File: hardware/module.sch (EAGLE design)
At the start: 118 parts, among them IC1 IC_USBLC6-2, IC2 LM1117IMPX-3.3, IC3 PIC32MX795F512, IC4 DP83848, IC5 LM1117MPX-2.5, U1 USD-SOCKETUSD, U2 VS1003, X2 CRYSTALS-NOGND-CFPX-217, X3 KUSBVX, Y3 CRYSTAL-GROUNDEDSMD-5X3.2

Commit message: Backlight fixed
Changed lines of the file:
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@@
 <pinref part="SV1" gate="G$1" pin="1"/>
 <wire x1="340.36" y1="243.84" x2="345.44" y2="243.84" width="0.1524" layer="91"/>
+<label x="345.44" y="243.84" size="1.4224" layer="95" xref="yes"/>
 </segment>
 </net>
@@
 <pinref part="SV1" gate="G$1" pin="2"/>
 <wire x1="325.12" y1="243.84" x2="320.04" y2="243.84" width="0.1524" layer="91"/>
+<label x="320.04" y="243.84" size="1.4224" layer="95" rot="R180" xref="yes"/>
 </segment>
 </net>

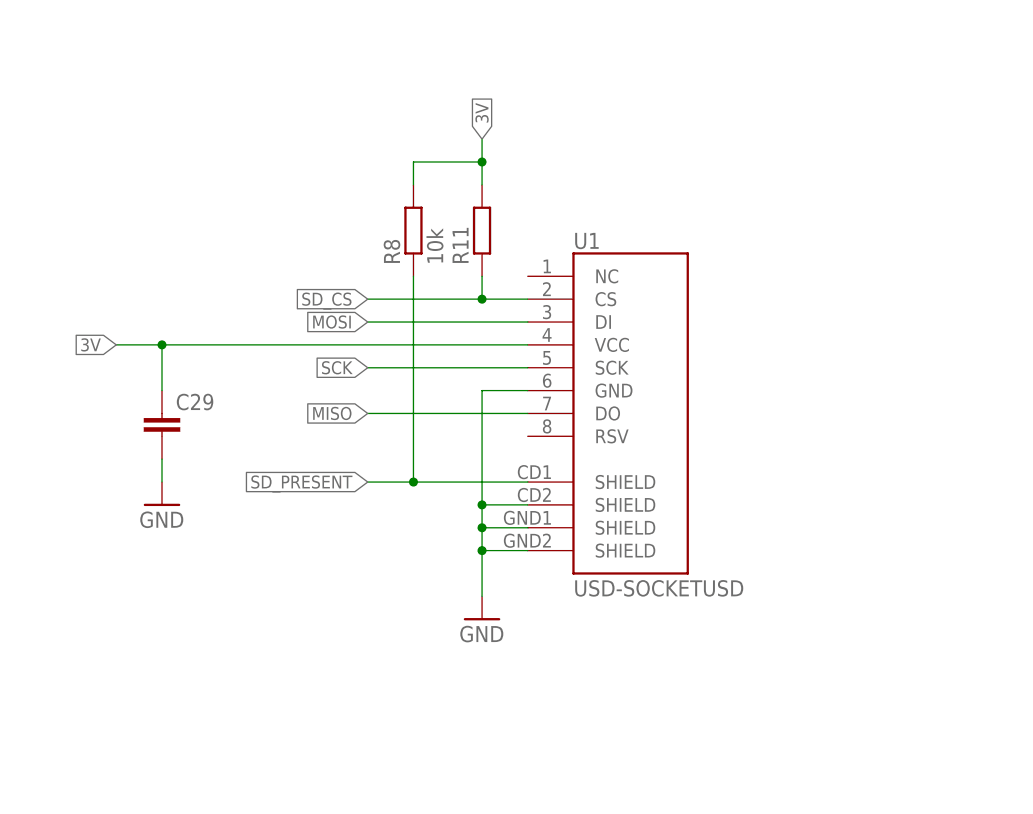
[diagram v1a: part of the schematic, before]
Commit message: MISO pull-up added
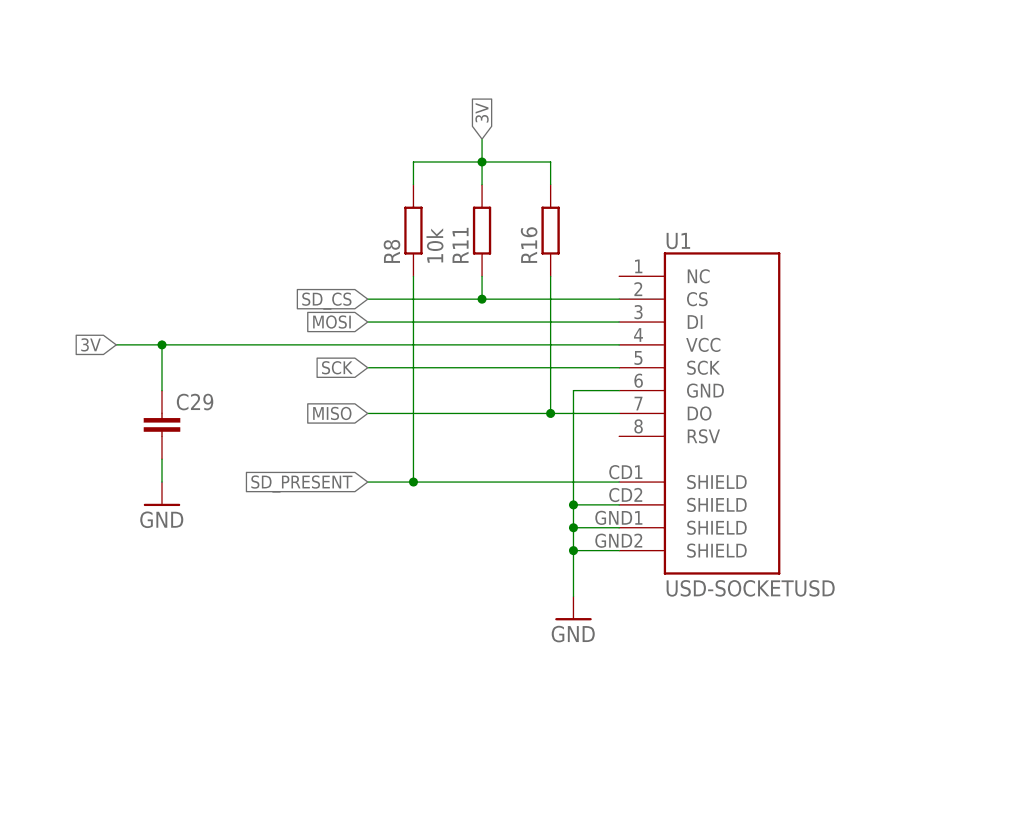
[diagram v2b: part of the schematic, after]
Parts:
- added R16: (no value), rcl:R-EU_R0603
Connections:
- net 3V: now also R16.2
- net MISO: now also R16.1
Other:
- moved on the sheet: U1
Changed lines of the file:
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@@
 <part name="GND3" library="SparkFun-Aesthetics" deviceset="GND" device=""/>
 <part name="L3" library="dp_devices" deviceset="FERRITE" device="-0805"/>
+<part name="R16" library="rcl" deviceset="R-EU_" device="R0603"/>
 </parts>
 <sheets>
@@
 <instance part="GND46" gate="1" x="132.08" y="60.96"/>
 <instance part="R13" gate="G$1" x="83.82" y="91.44" rot="R90"/>
-<instance part="U1" gate="G$1" x="254" y="81.28"/>
-<instance part="GND47" gate="1" x="241.3" y="55.88"/>
+<instance part="U1" gate="G$1" x="264.16" y="81.28"/>
+<instance part="GND47" gate="1" x="251.46" y="55.88"/>
 <instance part="R11" gate="G$1" x="241.3" y="99.06" rot="R90"/>
 <instance part="C29" gate="G$1" x="205.74" y="78.74"/>
@@
 <instance part="GND3" gate="1" x="0" y="535.94" rot="MR0"/>
 <instance part="L3" gate="L" x="419.1" y="-81.28"/>
+<instance part="R16" gate="G$1" x="248.92" y="99.06" rot="R90"/>
 </instances>
 <busses>
@@
 <pinref part="GND47" gate="1" pin="GND"/>
 <pinref part="U1" gate="G$1" pin="SHIELD@4"/>
-<wire x1="241.3" y1="66.04" x2="241.3" y2="63.5" width="0.1524" layer="91"/>
-<wire x1="241.3" y1="63.5" x2="241.3" y2="58.42" width="0.1524" layer="91"/>
-<wire x1="246.38" y1="63.5" x2="241.3" y2="63.5" width="0.1524" layer="91"/>
-<junction x="241.3" y="63.5"/>
+<wire x1="251.46" y1="66.04" x2="251.46" y2="63.5" width="0.1524" layer="91"/>
+<wire x1="251.46" y1="63.5" x2="251.46" y2="58.42" width="0.1524" layer="91"/>
+<wire x1="256.54" y1="63.5" x2="251.46" y2="63.5" width="0.1524" layer="91"/>
+<junction x="251.46" y="63.5"/>
 <pinref part="U1" gate="G$1" pin="SHIELD@3"/>
-<wire x1="246.38" y1="66.04" x2="241.3" y2="66.04" width="0.1524" layer="91"/>
-<junction x="241.3" y="66.04"/>
+<wire x1="256.54" y1="66.04" x2="251.46" y2="66.04" width="0.1524" layer="91"/>
+<junction x="251.46" y="66.04"/>
 <pinref part="U1" gate="G$1" pin="GND"/>
-<wire x1="246.38" y1="81.28" x2="241.3" y2="81.28" width="0.1524" layer="91"/>
-<wire x1="241.3" y1="81.28" x2="241.3" y2="68.58" width="0.1524" layer="91"/>
+<wire x1="256.54" y1="81.28" x2="251.46" y2="81.28" width="0.1524" layer="91"/>
+<wire x1="251.46" y1="81.28" x2="251.46" y2="68.58" width="0.1524" layer="91"/>
 <pinref part="U1" gate="G$1" pin="SHIELD@2"/>
-<wire x1="241.3" y1="68.58" x2="241.3" y2="66.04" width="0.1524" layer="91"/>
-<wire x1="246.38" y1="68.58" x2="241.3" y2="68.58" width="0.1524" layer="91"/>
-<junction x="241.3" y="68.58"/>
+<wire x1="251.46" y1="68.58" x2="251.46" y2="66.04" width="0.1524" layer="91"/>
+<wire x1="256.54" y1="68.58" x2="251.46" y2="68.58" width="0.1524" layer="91"/>
+<junction x="251.46" y="68.58"/>
 </segment>
 <segment>
@@
 <segment>
 <pinref part="U1" gate="G$1" pin="VCC"/>
-<wire x1="246.38" y1="86.36" x2="205.74" y2="86.36" width="0.1524" layer="91"/>
+<wire x1="256.54" y1="86.36" x2="205.74" y2="86.36" width="0.1524" layer="91"/>
 <pinref part="C29" gate="G$1" pin="1"/>
 <wire x1="205.74" y1="86.36" x2="200.66" y2="86.36" width="0.1524" layer="91"/>
@@
 <pinref part="R8" gate="G$1" pin="2"/>
 <wire x1="233.68" y1="106.68" x2="233.68" y2="104.14" width="0.1524" layer="91"/>
+<pinref part="R16" gate="G$1" pin="2"/>
+<wire x1="241.3" y1="106.68" x2="248.92" y2="106.68" width="0.1524" layer="91"/>
+<wire x1="248.92" y1="106.68" x2="248.92" y2="104.14" width="0.1524" layer="91"/>
 </segment>
 <segment>
@@
 <segment>
 <pinref part="U1" gate="G$1" pin="SCK"/>
-<wire x1="246.38" y1="83.82" x2="228.6" y2="83.82" width="0.1524" layer="91"/>
+<wire x1="256.54" y1="83.82" x2="228.6" y2="83.82" width="0.1524" layer="91"/>
 <label x="228.6" y="83.82" size="1.4224" layer="95" rot="R180" xref="yes"/>
 </segment>
@@
 <segment>
 <pinref part="U1" gate="G$1" pin="DO"/>
-<wire x1="246.38" y1="78.74" x2="228.6" y2="78.74" width="0.1524" layer="91"/>
+<wire x1="256.54" y1="78.74" x2="248.92" y2="78.74" width="0.1524" layer="91"/>
 <label x="228.6" y="78.74" size="1.4224" layer="95" rot="R180" xref="yes"/>
+<pinref part="R16" gate="G$1" pin="1"/>
+<wire x1="248.92" y1="78.74" x2="228.6" y2="78.74" width="0.1524" layer="91"/>
+<wire x1="248.92" y1="93.98" x2="248.92" y2="78.74" width="0.1524" layer="91"/>
+<junction x="248.92" y="78.74"/>
 </segment>
 <segment>
@@
 <segment>
 <pinref part="U1" gate="G$1" pin="DI"/>
-<wire x1="246.38" y1="88.9" x2="228.6" y2="88.9" width="0.1524" layer="91"/>
+<wire x1="256.54" y1="88.9" x2="228.6" y2="88.9" width="0.1524" layer="91"/>
 <label x="228.6" y="88.9" size="1.4224" layer="95" rot="R180" xref="yes"/>
 </segment>
@@
 <segment>
 <pinref part="U1" gate="G$1" pin="CS"/>
-<wire x1="246.38" y1="91.44" x2="241.3" y2="91.44" width="0.1524" layer="91"/>
+<wire x1="256.54" y1="91.44" x2="241.3" y2="91.44" width="0.1524" layer="91"/>
 <pinref part="R11" gate="G$1" pin="1"/>
 <wire x1="241.3" y1="91.44" x2="228.6" y2="91.44" width="0.1524" layer="91"/>
@@
 <segment>
 <pinref part="U1" gate="G$1" pin="SHIELD@1"/>
-<wire x1="246.38" y1="71.12" x2="233.68" y2="71.12" width="0.1524" layer="91"/>
+<wire x1="256.54" y1="71.12" x2="233.68" y2="71.12" width="0.1524" layer="91"/>
 <label x="228.6" y="71.12" size="1.4224" layer="95" rot="R180" xref="yes"/>
 <pinref part="R8" gate="G$1" pin="1"/>

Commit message: Fixes
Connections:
- removed net LED: SV1.6
- net RA15_ROT_SW: now also SV1.6
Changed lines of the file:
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@@
-</segment>
-</net>
-<net name="LED" class="0">
-<segment>
-<pinref part="SV1" gate="G$1" pin="6"/>
-<wire x1="325.12" y1="248.92" x2="320.04" y2="248.92" width="0.1524" layer="91"/>
-<label x="320.04" y="248.92" size="1.4224" layer="95" rot="R180" xref="yes"/>
 </segment>
 </net>
@@
 <label x="15.24" y="406.4" size="1.4224" layer="95" rot="R180" xref="yes"/>
 </segment>
-</net>
+<segment>
+<pinref part="SV1" gate="G$1" pin="6"/>
+<wire x1="325.12" y1="248.92" x2="320.04" y2="248.92" width="0.1524" layer="91"/>
+<label x="320.04" y="248.92" size="1.4224" layer="95" rot="R180" xref="yes"/>
+</segment>
+</net>
